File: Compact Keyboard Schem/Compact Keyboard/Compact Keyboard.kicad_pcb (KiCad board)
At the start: 2 copper layers, 105.5 x 115.1 mm, 41 parts, among them J1 MUX+POT, J2 MUX Power, J4 PAM8406 Power, J5 ILI 9341, J6 USB_A, J7 Rotary_Encoder, J8 USB_Host, J9 Jack-DC, Q1 Q_PMOS_GSD, Q2 Q_PMOS_GSD, SW1 SW_Push_LED, SW2 SW_Push, SW3 SW_Push, SW4 SW_Push, SW5 SW_Push

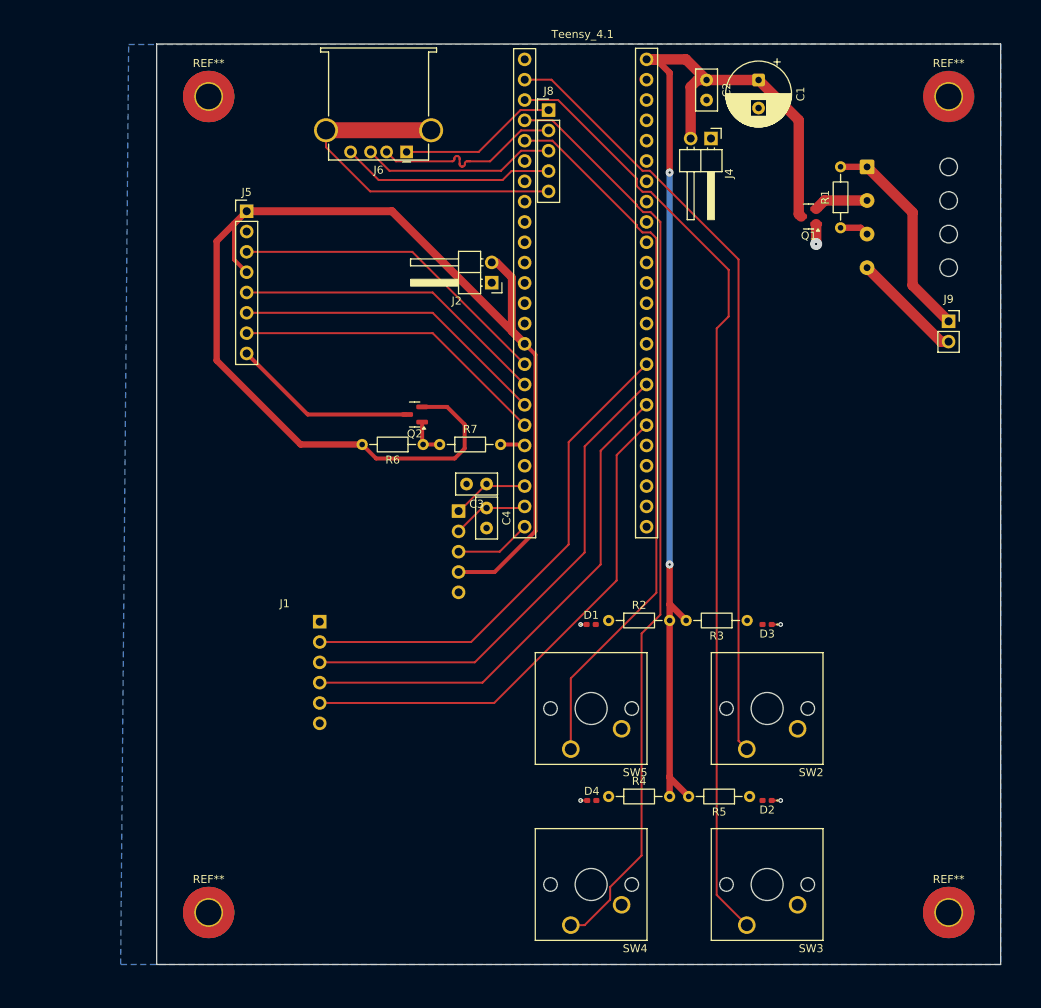
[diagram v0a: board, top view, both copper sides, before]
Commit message: Post PCB Manufacturing
Specifically the Potentiometer+ MUX
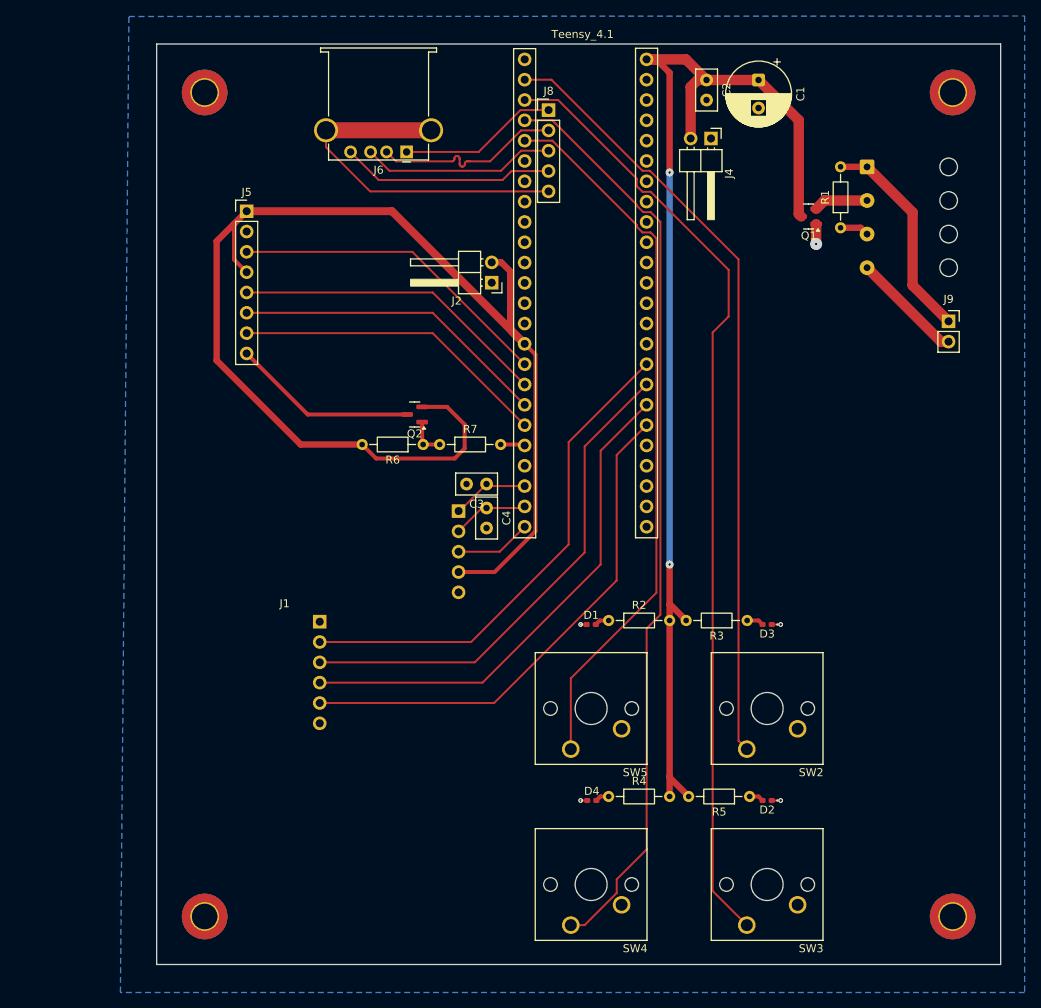
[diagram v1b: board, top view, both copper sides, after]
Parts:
- removed ? (x6): , 
- removed the REF** at (102.0, 134.0)
- removed the REF** at (194.5, 32.0)
- removed the REF** at (194.5, 134.0)
- removed the REF** at (102.0, 32.0)
- added REF**: MountingHole_3.2mm_M3_ISO7380_Pad_TopBottom, MountingHole:MountingHole_3.2mm_M3_ISO7380_Pad_TopBottom, F.Cu at (101.5, 31.5)
- added REF**: MountingHole_3.2mm_M3_ISO7380_Pad_TopBottom, MountingHole:MountingHole_3.2mm_M3_ISO7380_Pad_TopBottom, F.Cu at (101.5, 134.5)
- added REF**: MountingHole_3.2mm_M3_ISO7380_Pad_TopBottom, MountingHole:MountingHole_3.2mm_M3_ISO7380_Pad_TopBottom, F.Cu at (195.0, 134.5)
- added REF**: MountingHole_3.2mm_M3_ISO7380_Pad_TopBottom, MountingHole:MountingHole_3.2mm_M3_ISO7380_Pad_TopBottom, F.Cu at (195.0, 31.5)
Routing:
- net +3.3V: track 162.3 -> 164.9 mm
- net Net-(D3-A): track 0.00 -> 2.13 mm
- net Net-(D2-A): track 0.00 -> 1.82 mm
- net Net-(D1-A): track 0.00 -> 1.82 mm
- net Net-(D4-A): track 0.00 -> 1.74 mm

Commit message: Pushing Update
Latest version after PCB printing
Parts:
- removed J5: ILI 9341, Connector_PinHeader_2.54mm:PinHeader_1x08_P2.54mm_Vertical
- removed J7: Rotary_Encoder, Connector_PinHeader_2.54mm:PinHeader_1x05_P2.54mm_Horizontal
- removed Q1: Q_PMOS_GSD, Package_TO_SOT_SMD:SOT-23
- added 10k: 10K, Resistor_SMD:R_0805_2012Metric_Pad1.20x1.40mm_HandSolder, F.Cu at (144.3, 83.3)
- added 10k: 10K, Resistor_SMD:R_0805_2012Metric_Pad1.20x1.40mm_HandSolder, F.Cu at (144.3, 79.5)
- added 10k: 10K, Resistor_SMD:R_0805_2012Metric_Pad1.20x1.40mm_HandSolder, F.Cu at (144.3, 75.7)
- added J3: SW_Switch_LED, Connector_Wire:SolderWire-0.25sqmm_1x04_P4.2mm_D0.65mm_OD1.7mm_Relief, B.Cu at (184.5, 39.7)
- added Q3: Q_PMOS_GDS, Package_TO_SOT_THT:TO-220F-3_Vertical, F.Cu at (171.5, 40.9)
- added TFT_ILI1: ~, TOMD:ILI9341_TFT, B.Cu at (140.4, 40.5)
- 10k: renamed from R6; footprint Resistor_THT:R_Axial_DIN0204_L3.6mm_D1.6mm_P7.62mm_Horizontal -> Resistor_SMD:R_0805_2012Metric_Pad1.20x1.40mm_HandSolder
- 1k: renamed from R7; footprint Resistor_THT:R_Axial_DIN0204_L3.6mm_D1.6mm_P7.62mm_Horizontal -> Resistor_SMD:R_0805_2012Metric_Pad1.20x1.40mm_HandSolder
- 220R: renamed from R1; footprint Resistor_THT:R_Axial_DIN0204_L3.6mm_D1.6mm_P7.62mm_Horizontal -> Resistor_SMD:R_0805_2012Metric_Pad1.20x1.40mm_HandSolder
- 220R: renamed from R5; footprint Resistor_THT:R_Axial_DIN0204_L3.6mm_D1.6mm_P7.62mm_Horizontal -> Resistor_SMD:R_0805_2012Metric_Pad1.20x1.40mm_HandSolder; moved to B.Cu
- 220R: renamed from R4; footprint Resistor_THT:R_Axial_DIN0204_L3.6mm_D1.6mm_P7.62mm_Horizontal -> Resistor_SMD:R_0805_2012Metric_Pad1.20x1.40mm_HandSolder; moved to B.Cu
- 220R: renamed from R2; footprint Resistor_THT:R_Axial_DIN0204_L3.6mm_D1.6mm_P7.62mm_Horizontal -> Resistor_SMD:R_0805_2012Metric_Pad1.20x1.40mm_HandSolder; moved to B.Cu
- 220R: renamed from R3; footprint Resistor_THT:R_Axial_DIN0204_L3.6mm_D1.6mm_P7.62mm_Horizontal -> Resistor_SMD:R_0805_2012Metric_Pad1.20x1.40mm_HandSolder; moved to B.Cu
- D1, D2, D3, D4: footprint LED_SMD:LED_0402_1005Metric_Pad0.77x0.64mm_HandSolder -> LED_SMD:LED_0805_2012Metric_Pad1.15x1.40mm_HandSolder; moved to B.Cu
- J1: moved to F.Cu
- SW1: value SW_Push_LED -> RotaryEncoder_Switch_MP; footprint Connector_Wire:SolderWire-0.25sqmm_1x04_P4.2mm_D0.65mm_OD1.7mm_Relief -> Rotary_Encoder:RotaryEncoder_Alps_EC11E-Switch_Vertical_H20mm
- SW2, SW3, SW4, SW5: moved to B.Cu
- moved SW1 85.6 mm to (123.5, 101.0), turned to 180 degrees
- moved D4 39.6 mm to (187.7, 108.2), turned to 180 degrees
- moved D1 38.9 mm to (187.7, 89.2), turned to 180 degrees
- moved 220R 33.9 mm to (183.9, 108.2), turned to 180 degrees
- moved 220R 33.0 mm to (183.9, 89.2), turned to 180 degrees
- moved J1 29.7 mm to (144.3, 106.2)
- moved SW4 27.2 mm to (171.2, 122.7), turned to 0 degrees
- moved SW5 25.9 mm to (171.2, 103.6), turned to 0 degrees
- moved SW3 24.6 mm to (190.2, 122.7), turned to 0 degrees
- moved SW2 23.2 mm to (190.2, 103.6), turned to 0 degrees
- moved J4 13.5 mm to (160.4, 50.0), turned to 0 degrees
- moved 10k 13.0 mm to (133.2, 63.2), turned to 0 degrees
- moved REF** 12.5 mm to (89.0, 31.5)
- moved REF** 12.5 mm to (89.0, 134.5)
- moved D2 12.2 mm to (168.7, 108.2), turned to 0 degrees
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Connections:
- 220R pad 1: Net-(SW1-K) -> Net-(J3-Pin_2)
- 220R pad 2: Net-(J9-Pad1) -> Net-(J3-Pin_1)
- J1 pad 2: /SIG_MUX -> /S0_MUX
- J1 pad 3: /S2_MUX -> /S1_MUX
- J1 pad 4: /S1_MUX -> /S2_MUX
- J1 pad 5: /S0_MUX -> /SIG_MUX
- J9 pad 1: Net-(J9-Pad1) -> Net-(J3-Pin_1)
- Teensy_4.1 pad 16: /ILI_9341/CS_LCD -> unconnected-(Teensy_4.1-24-Pad16)
- Teensy_4.1 pad 17: /ILI_9341/DC_LCD -> /ILI_9341/LED_LCD
- Teensy_4.1 pad 20: /ILI_9341/LED_LCD -> /ILI_9341/DC_LCD
- Teensy_4.1 pad 21: unconnected-(Teensy_4.1-29-Pad21) -> /ILI_9341/CS_LCD
- Teensy_4.1 pad 22: /Rotary_Encoder/CLK_RE -> /Rotary_Encoder/SW_RE
- Teensy_4.1 pad 24: /Rotary_Encoder/SW_RE -> /Rotary_Encoder/CLK_RE
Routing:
- net /Rotary_Encoder/SW_RE: track 9.55 -> 51.9 mm
- net /S0_MUX: track 64.4 -> 35.7 mm
- net /S1_MUX: track 63.6 -> 35.7 mm
- net Net-(J3-Pin_1): track 0.00 -> 27.4 mm
- net /S2_MUX: track 63.0 -> 35.7 mm
- net /SIG_MUX: track 62.7 -> 35.7 mm
- net Net-(J9-Pad1): track 26.8 -> 0.00 mm
- net +3.3V: track 164.9 -> 142.2 mm
- net /Rotary_Encoder/DT_RE: track 9.55 -> 32.0 mm
- net /Rotary_Encoder/CLK_RE: track 9.77 -> 31.0 mm
- net GND: track 20.3 -> 0.00 mm, vias 5 -> 0
- net Net-(J3-Pin_4): track 0.00 -> 14.7 mm
- net /Buttons/BTN3_IN: track 115.8 -> 105.7 mm
- net /Buttons/BTN4_IN: track 89.9 -> 81.0 mm
- net /ILI_9341/MOSI_LCD: track 39.5 -> 47.4 mm, vias 0 -> 2
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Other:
- board size 105.5 x 115.1 mm -> 118 x 115.1 mm
- board text added: "+5V"
- board text added: "3.3V"
- board text added: "S0"
- board text added: "S1"
- board text added: "S2"
- board text added: "SIG"
